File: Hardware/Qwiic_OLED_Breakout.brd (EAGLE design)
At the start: 27.3 x 29.7 mm, 45 parts, among them J1 QWIIC_RIGHT_ANGLE, J2 QWIIC_RIGHT_ANGLE

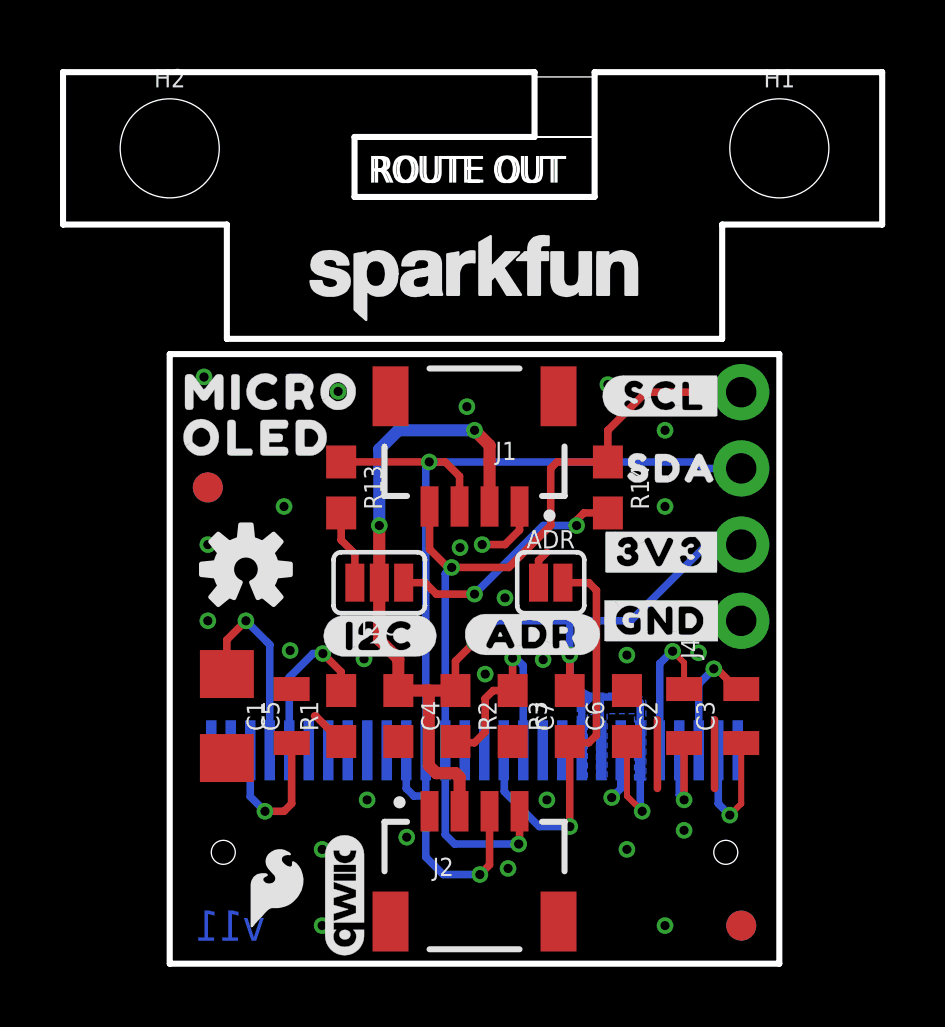
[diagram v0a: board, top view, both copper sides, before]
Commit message: Adds new panel after bringing the tabbed part to match the panel
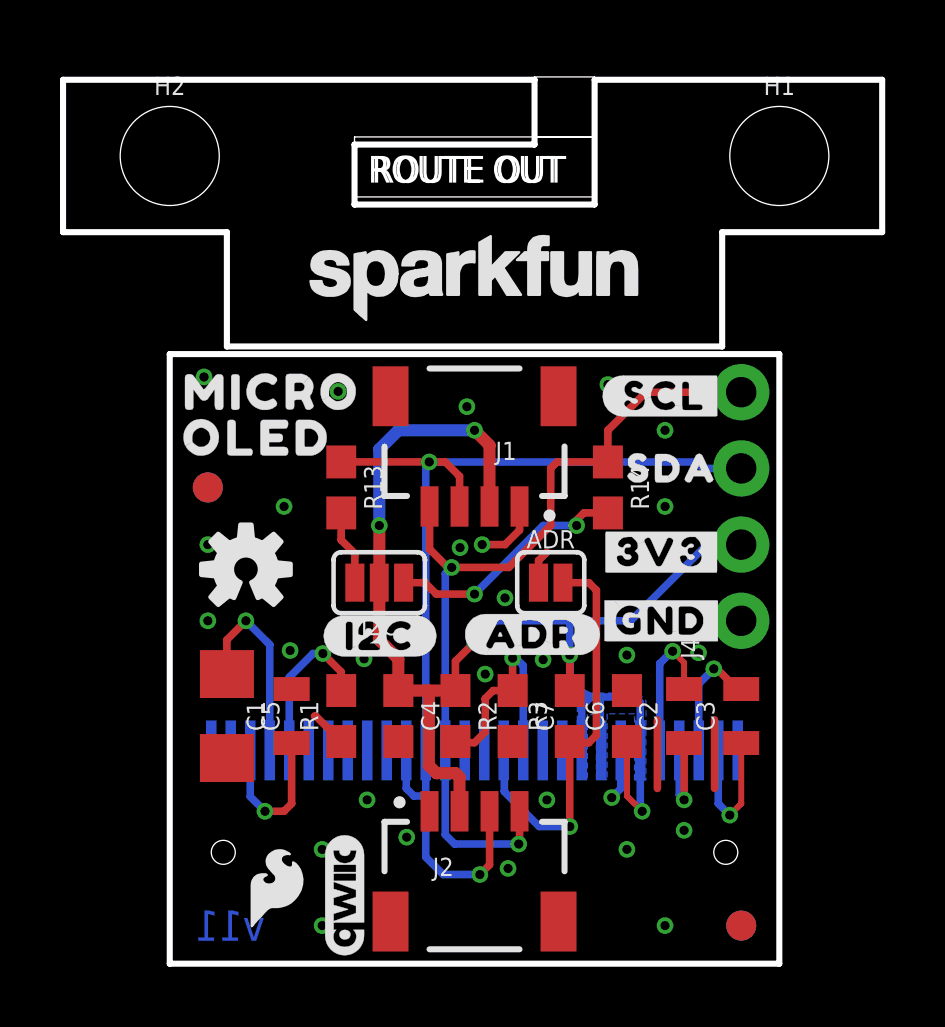
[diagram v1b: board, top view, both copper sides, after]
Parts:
- moved H1 0.25 mm to (20.3, 26.9)
- moved H2 0.25 mm to (0.00, 26.9)
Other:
- board size 27.3 x 29.7 mm -> 27.3 x 29.6 mm
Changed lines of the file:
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@@
 <setting verticaltext="up"/>
 </settings>
-<grid distance="0.05" unitdist="inch" unit="inch" style="dots" multiple="1" display="yes" altdistance="0.001" altunitdist="inch" altunit="inch"/>
+<grid distance="0.05" unitdist="inch" unit="inch" style="dots" multiple="1" display="yes" altdistance="0.005" altunitdist="inch" altunit="inch"/>
 <layers>
 <layer number="1" name="Top" color="4" fill="1" visible="yes" active="yes"/>
@@
 <layer number="45" name="Holes" color="7" fill="1" visible="yes" active="yes"/>
 <layer number="46" name="Milling" color="3" fill="1" visible="no" active="yes"/>
-<layer number="47" name="Measures" color="7" fill="1" visible="yes" active="yes"/>
+<layer number="47" name="Measures" color="7" fill="1" visible="no" active="yes"/>
 <layer number="48" name="Document" color="7" fill="1" visible="no" active="yes"/>
 <layer number="49" name="Reference" color="13" fill="1" visible="yes" active="yes"/>
@@
 <wire x1="0" y1="20.32" x2="0" y2="0" width="0.2032" layer="20"/>
 <wire x1="0" y1="0" x2="20.32" y2="0" width="0.2032" layer="20"/>
-<wire x1="-3.556" y1="29.718" x2="-3.556" y2="24.638" width="0.2032" layer="20"/>
-<wire x1="-3.556" y1="24.638" x2="1.905" y2="24.638" width="0.2032" layer="20"/>
-<wire x1="18.415" y1="24.638" x2="23.749" y2="24.638" width="0.2032" layer="20"/>
-<wire x1="23.749" y1="24.638" x2="23.749" y2="29.718" width="0.2032" layer="20"/>
+<wire x1="-3.556" y1="29.464" x2="-3.556" y2="24.384" width="0.2032" layer="20"/>
+<wire x1="-3.556" y1="24.384" x2="1.905" y2="24.384" width="0.2032" layer="20"/>
+<wire x1="18.415" y1="24.384" x2="23.749" y2="24.384" width="0.2032" layer="20"/>
+<wire x1="23.749" y1="24.384" x2="23.749" y2="29.464" width="0.2032" layer="20"/>
 <rectangle x1="6.16" y1="25.558" x2="14.16" y2="27.558" layer="46" rot="R180"/>
 <rectangle x1="12.16" y1="27.558" x2="14.16" y2="29.558" layer="46" rot="R180"/>
-<wire x1="12.16" y1="29.718" x2="12.16" y2="27.558" width="0.2032" layer="20"/>
-<wire x1="12.16" y1="27.558" x2="6.16" y2="27.558" width="0.2032" layer="20"/>
-<wire x1="6.16" y1="27.558" x2="6.16" y2="25.558" width="0.2032" layer="20"/>
-<wire x1="6.16" y1="25.558" x2="14.16" y2="25.558" width="0.2032" layer="20"/>
-<wire x1="12.16" y1="29.718" x2="-3.556" y2="29.718" width="0.2032" layer="20"/>
-<wire x1="14.163040625" y1="25.562559375" x2="14.163040625" y2="29.718" width="0.2032" layer="20"/>
-<wire x1="14.163040625" y1="29.718" x2="23.749" y2="29.718" width="0.2032" layer="20"/>
+<wire x1="12.16" y1="29.464" x2="12.16" y2="27.304" width="0.2032" layer="20"/>
+<wire x1="12.16" y1="27.304" x2="6.16" y2="27.304" width="0.2032" layer="20"/>
+<wire x1="6.16" y1="27.304" x2="6.16" y2="25.304" width="0.2032" layer="20"/>
+<wire x1="6.16" y1="25.304" x2="14.16" y2="25.304" width="0.2032" layer="20"/>
+<wire x1="12.16" y1="29.464" x2="-3.556" y2="29.464" width="0.2032" layer="20"/>
+<wire x1="14.163040625" y1="25.308559375" x2="14.163040625" y2="29.464" width="0.2032" layer="20"/>
+<wire x1="14.163040625" y1="29.464" x2="23.749" y2="29.464" width="0.2032" layer="20"/>
 <text x="12.7" y="-27.94" size="1.778" layer="51" font="vector">Joel Bartlett</text>
 <dimension x1="-3.81" y1="29.718" x2="-3.81" y2="0" x3="-15.24" y3="14.859" textsize="1.778" layer="47" unit="inch"/>
@@
 <dimension x1="0" y1="0" x2="0" y2="27.178" x3="-11.43" y3="13.589" textsize="1.778" layer="47" unit="inch"/>
 <text x="11.43" y="-30.5054" size="1.778" layer="51" font="vector">Andy England, Elias Santistevan</text>
-<wire x1="1.905" y1="24.638" x2="1.905" y2="20.828" width="0.2032" layer="20"/>
-<wire x1="1.905" y1="20.828" x2="18.415" y2="20.828" width="0.2032" layer="20"/>
-<wire x1="18.415" y1="20.828" x2="18.415" y2="24.638" width="0.2032" layer="20"/>
+<wire x1="1.905" y1="24.384" x2="1.905" y2="20.574" width="0.2032" layer="20"/>
+<wire x1="1.905" y1="20.574" x2="18.415" y2="20.574" width="0.2032" layer="20"/>
+<wire x1="18.415" y1="20.574" x2="18.415" y2="24.384" width="0.2032" layer="20"/>
 <wire x1="0" y1="20.32" x2="20.32" y2="20.32" width="0.2032" layer="20"/>
 <text x="6.731" y="26.035" size="0.889" layer="46" font="vector" ratio="12">ROUTE OUT</text>
@@
 <attribute name="VALUE" x="6.985" y="13.843" size="0.6096" layer="27" font="vector" ratio="20" rot="R180" align="top-center"/>
 </element>
-<element name="H1" library="SparkFun-Hardware" package="STAND-OFF" value="STAND-OFF" x="20.32" y="27.178" smashed="yes">
-<attribute name="NAME" x="20.32" y="29.21" size="0.6096" layer="25" font="vector" ratio="20" align="bottom-center"/>
-<attribute name="VALUE" x="20.32" y="25.146" size="0.6096" layer="27" font="vector" ratio="20" align="top-center"/>
-</element>
-<element name="H2" library="SparkFun-Hardware" package="STAND-OFF" value="STAND-OFF" x="0" y="27.178" smashed="yes">
-<attribute name="NAME" x="0" y="29.21" size="0.6096" layer="25" font="vector" ratio="20" align="bottom-center"/>
-<attribute name="VALUE" x="0" y="25.146" size="0.6096" layer="27" font="vector" ratio="20" align="top-center"/>
+<element name="H1" library="SparkFun-Hardware" package="STAND-OFF" value="STAND-OFF" x="20.32" y="26.924" smashed="yes">
+<attribute name="NAME" x="20.32" y="28.956" size="0.6096" layer="25" font="vector" ratio="20" align="bottom-center"/>
+<attribute name="VALUE" x="20.32" y="24.892" size="0.6096" layer="27" font="vector" ratio="20" align="top-center"/>
+</element>
+<element name="H2" library="SparkFun-Hardware" package="STAND-OFF" value="STAND-OFF" x="0" y="26.924" smashed="yes">
+<attribute name="NAME" x="0" y="28.956" size="0.6096" layer="25" font="vector" ratio="20" align="bottom-center"/>
+<attribute name="VALUE" x="0" y="24.892" size="0.6096" layer="27" font="vector" ratio="20" align="top-center"/>
 </element>
 <element name="ADR" library="SparkFun-Jumpers" package="SMT-JUMPER_2_NO_SILK" package3d_urn="urn:adsk.eagle:package:39279/1" value="JUMPER-SMT_2_NO_SILK" x="12.7" y="12.7" smashed="yes">
